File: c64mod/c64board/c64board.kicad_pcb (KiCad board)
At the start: 2 copper layers, 24.1 x 53.3 mm, 12 parts, among them J1 Conn_02x10_Odd_Even, U1 VIC-II, U2 MIC5504-3.3YM5, U3 LVC257, U4 LVC245, U5 LVC245

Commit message: Finished C64 mod board
generate gerber files also for Rev. 1
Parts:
- added REF**: OSHW-Logo2_7.3x6mm_SilkScreen, Symbol:OSHW-Logo2_7.3x6mm_SilkScreen, B.Cu at (143.8, 59.2)
- moved J1 23.0 mm to (154.9, 91.4), turned to 180 degrees
- moved R1 0.76 mm to (153.2, 99.1)
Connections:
- C2 pad 2: Net-(C2-Pad2) -> GND
- C3 pad 2: Net-(C2-Pad2) -> GND
- C4 pad 2: Net-(C2-Pad2) -> GND
- C5 pad 2: Net-(C2-Pad2) -> GND
- J1 pad 1: DB7 -> PHI0
- J1 pad 10: DB10_A4 -> DB9_A3
- J1 pad 11: DB9_A3 -> DB10_A4
- J1 pad 12: DB8_A2 -> DB11_A5
- J1 pad 13: A1 -> DB0
- J1 pad 14: A0 -> DB1
- J1 pad 15: CS -> DB2
- J1 pad 16: RW -> DB3
- J1 pad 17: BA -> DB4
- J1 pad 18: AEC -> DB5
- J1 pad 19: GND -> DB6
- J1 pad 2: DB6 -> GND
- J1 pad 20: PHI0 -> DB7
- J1 pad 3: DB5 -> AEC
- J1 pad 4: DB4 -> BA
- J1 pad 5: DB3 -> RW
- J1 pad 6: DB2 -> CS
- J1 pad 7: DB1 -> A0
- J1 pad 8: DB0 -> A1
- J1 pad 9: DB11_A5 -> DB8_A2
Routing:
- net Net-(U1-Pad27): track 0.00 -> 18.9 mm, vias 0 -> 3
- net GND: track 8.83 -> 27.2 mm, vias 3 -> 12
- net Net-(U1-Pad26): track 0.00 -> 15.4 mm, vias 0 -> 3
- net DB11_A5: track 0.00 -> 15.1 mm, vias 0 -> 1
- net DB9_A3: track 0.00 -> 14.3 mm, vias 0 -> 1
- net Net-(U1-Pad28): track 0.00 -> 13.9 mm, vias 0 -> 1
- net DB10_A4: track 0.00 -> 10.9 mm, vias 0 -> 2
- net +3V3: track 68.7 -> 65.7 mm
- net DB0: track 15.5 -> 18.4 mm
- net DB7: track 15.9 -> 13.7 mm
- net Net-(U1-Pad36): track 26.7 -> 25.5 mm
- net Net-(U1-Pad29): track 15.5 -> 16.7 mm
- net PHI0: track 7.01 -> 8.08 mm
- net BA: track 16.7 -> 15.7 mm
- net AEC: track 42.2 -> 41.6 mm
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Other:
- board text added: "1"
- board text added: "C64 mod Rev 1 github.com/c0pperdragon"

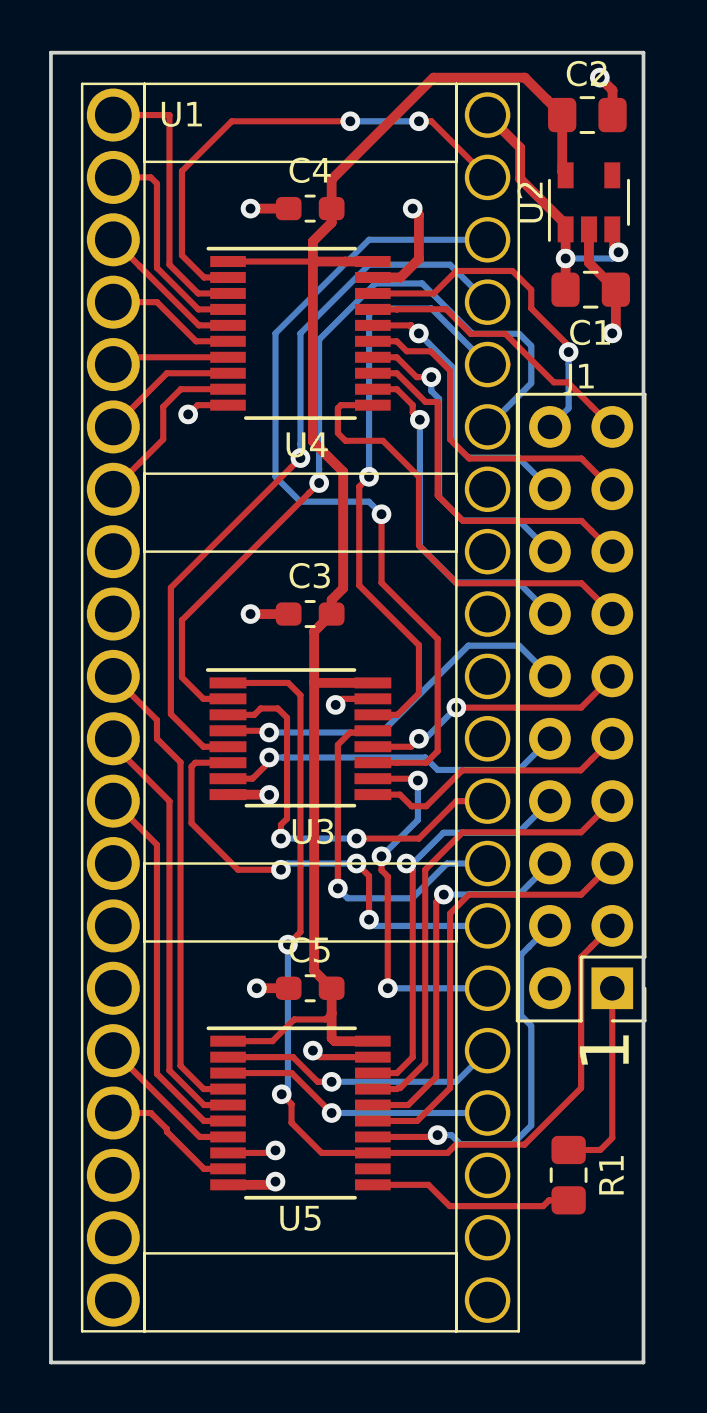
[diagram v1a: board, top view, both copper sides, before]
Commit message: Reverse connector orientation
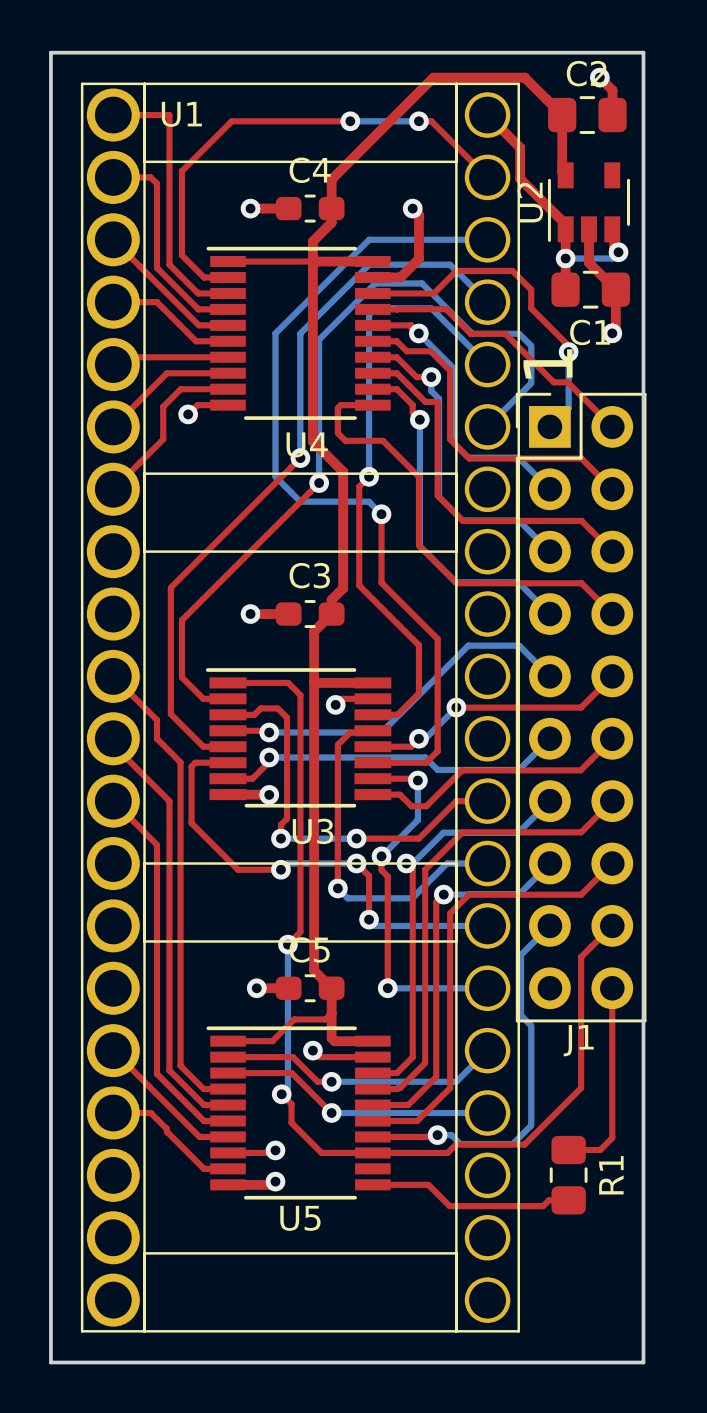
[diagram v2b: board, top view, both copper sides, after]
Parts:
- moved J1 23.0 mm to (152.4, 68.6), turned to 0 degrees
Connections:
- J1 pad 1: PHI0 -> DB7
- J1 pad 10: DB9_A3 -> DB10_A4
- J1 pad 11: DB10_A4 -> DB9_A3
- J1 pad 12: DB11_A5 -> DB8_A2
- J1 pad 13: DB0 -> A1
- J1 pad 14: DB1 -> A0
- J1 pad 15: DB2 -> CS
- J1 pad 16: DB3 -> RW
- J1 pad 17: DB4 -> BA
- J1 pad 18: DB5 -> AEC
- J1 pad 19: DB6 -> GND
- J1 pad 2: GND -> DB6
- J1 pad 20: DB7 -> PHI0
- J1 pad 3: AEC -> DB5
- J1 pad 4: BA -> DB4
- J1 pad 5: RW -> DB3
- J1 pad 6: CS -> DB2
- J1 pad 7: A0 -> DB1
- J1 pad 8: A1 -> DB0
- J1 pad 9: DB8_A2 -> DB11_A5
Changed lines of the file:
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@@
   )
   (module Connector_PinHeader_2.54mm:PinHeader_2x10_P2.54mm_Vertical (layer F.Cu)
-    (at 154.94 91.44 180)
+    (at 152.4 68.58)
     (descr "Through hole straight pin header, 2x10, 2.54mm pitch, double rows")
     (tags "Through hole pin header THT 2x10 2.54mm double row")
-    (fp_text reference J1 (at 1.27 24.892 180) (layer F.SilkS)
-      (effects (font (size 1 1) (thickness 0.15)))
-    )
-    (fp_text value Conn_02x10_Odd_Even (at 1.27 25.19 180) (layer F.Fab)
+    (fp_text reference J1 (at 1.27 24.892) (layer F.SilkS)
+      (effects (font (size 1 1) (thickness 0.15)))
+    )
+    (fp_text value Conn_02x10_Odd_Even (at 1.27 25.19) (layer F.Fab)
       (effects (font (size 1 1) (thickness 0.15)))
     )
@@
     (fp_line (start 4.35 24.65) (end 4.35 -1.8) (layer F.CrtYd) (width 0.05))
     (fp_line (start 4.35 -1.8) (end -1.8 -1.8) (layer F.CrtYd) (width 0.05))
-    (fp_text user %R (at 1.27 11.43 270) (layer F.Fab)
-      (effects (font (size 1 1) (thickness 0.15)))
-    )
-    (pad 1 thru_hole rect (at 0 0 180) (size 1.7 1.7) (drill 1) (layers *.Cu *.Mask)
+    (fp_text user %R (at 1.27 11.43 90) (layer F.Fab)
+      (effects (font (size 1 1) (thickness 0.15)))
+    )
+    (pad 1 thru_hole rect (at 0 0) (size 1.7 1.7) (drill 1) (layers *.Cu *.Mask)
+      (net 4 DB7))
+    (pad 2 thru_hole oval (at 2.54 0) (size 1.7 1.7) (drill 1) (layers *.Cu *.Mask)
+      (net 5 DB6))
+    (pad 3 thru_hole oval (at 0 2.54) (size 1.7 1.7) (drill 1) (layers *.Cu *.Mask)
+      (net 6 DB5))
+    (pad 4 thru_hole oval (at 2.54 2.54) (size 1.7 1.7) (drill 1) (layers *.Cu *.Mask)
+      (net 7 DB4))
+    (pad 5 thru_hole oval (at 0 5.08) (size 1.7 1.7) (drill 1) (layers *.Cu *.Mask)
+      (net 8 DB3))
+    (pad 6 thru_hole oval (at 2.54 5.08) (size 1.7 1.7) (drill 1) (layers *.Cu *.Mask)
+      (net 9 DB2))
+    (pad 7 thru_hole oval (at 0 7.62) (size 1.7 1.7) (drill 1) (layers *.Cu *.Mask)
+      (net 10 DB1))
+    (pad 8 thru_hole oval (at 2.54 7.62) (size 1.7 1.7) (drill 1) (layers *.Cu *.Mask)
+      (net 11 DB0))
+    (pad 9 thru_hole oval (at 0 10.16) (size 1.7 1.7) (drill 1) (layers *.Cu *.Mask)
+      (net 12 DB11_A5))
+    (pad 10 thru_hole oval (at 2.54 10.16) (size 1.7 1.7) (drill 1) (layers *.Cu *.Mask)
+      (net 13 DB10_A4))
+    (pad 11 thru_hole oval (at 0 12.7) (size 1.7 1.7) (drill 1) (layers *.Cu *.Mask)
+      (net 14 DB9_A3))
+    (pad 12 thru_hole oval (at 2.54 12.7) (size 1.7 1.7) (drill 1) (layers *.Cu *.Mask)
+      (net 15 DB8_A2))
+    (pad 13 thru_hole oval (at 0 15.24) (size 1.7 1.7) (drill 1) (layers *.Cu *.Mask)
+      (net 16 A1))
+    (pad 14 thru_hole oval (at 2.54 15.24) (size 1.7 1.7) (drill 1) (layers *.Cu *.Mask)
+      (net 17 A0))
+    (pad 15 thru_hole oval (at 0 17.78) (size 1.7 1.7) (drill 1) (layers *.Cu *.Mask)
+      (net 18 CS))
+    (pad 16 thru_hole oval (at 2.54 17.78) (size 1.7 1.7) (drill 1) (layers *.Cu *.Mask)
+      (net 19 RW))
+    (pad 17 thru_hole oval (at 0 20.32) (size 1.7 1.7) (drill 1) (layers *.Cu *.Mask)
+      (net 20 BA))
+    (pad 18 thru_hole oval (at 2.54 20.32) (size 1.7 1.7) (drill 1) (layers *.Cu *.Mask)
+      (net 21 AEC))
+    (pad 19 thru_hole oval (at 0 22.86) (size 1.7 1.7) (drill 1) (layers *.Cu *.Mask)
+      (net 2 GND))
+    (pad 20 thru_hole oval (at 2.54 22.86) (size 1.7 1.7) (drill 1) (layers *.Cu *.Mask)
       (net 22 PHI0))
-    (pad 2 thru_hole oval (at 2.54 0 180) (size 1.7 1.7) (drill 1) (layers *.Cu *.Mask)
-      (net 2 GND))
-    (pad 3 thru_hole oval (at 0 2.54 180) (size 1.7 1.7) (drill 1) (layers *.Cu *.Mask)
-      (net 21 AEC))
-    (pad 4 thru_hole oval (at 2.54 2.54 180) (size 1.7 1.7) (drill 1) (layers *.Cu *.Mask)
-      (net 20 BA))
-    (pad 5 thru_hole oval (at 0 5.08 180) (size 1.7 1.7) (drill 1) (layers *.Cu *.Mask)
-      (net 19 RW))
-    (pad 6 thru_hole oval (at 2.54 5.08 180) (size 1.7 1.7) (drill 1) (layers *.Cu *.Mask)
-      (net 18 CS))
-    (pad 7 thru_hole oval (at 0 7.62 180) (size 1.7 1.7) (drill 1) (layers *.Cu *.Mask)
-      (net 17 A0))
-    (pad 8 thru_hole oval (at 2.54 7.62 180) (size 1.7 1.7) (drill 1) (layers *.Cu *.Mask)
-      (net 16 A1))
-    (pad 9 thru_hole oval (at 0 10.16 180) (size 1.7 1.7) (drill 1) (layers *.Cu *.Mask)
-      (net 15 DB8_A2))
-    (pad 10 thru_hole oval (at 2.54 10.16 180) (size 1.7 1.7) (drill 1) (layers *.Cu *.Mask)
-      (net 14 DB9_A3))
-    (pad 11 thru_hole oval (at 0 12.7 180) (size 1.7 1.7) (drill 1) (layers *.Cu *.Mask)
-      (net 13 DB10_A4))
-    (pad 12 thru_hole oval (at 2.54 12.7 180) (size 1.7 1.7) (drill 1) (layers *.Cu *.Mask)
-      (net 12 DB11_A5))
-    (pad 13 thru_hole oval (at 0 15.24 180) (size 1.7 1.7) (drill 1) (layers *.Cu *.Mask)
-      (net 11 DB0))
-    (pad 14 thru_hole oval (at 2.54 15.24 180) (size 1.7 1.7) (drill 1) (layers *.Cu *.Mask)
-      (net 10 DB1))
-    (pad 15 thru_hole oval (at 0 17.78 180) (size 1.7 1.7) (drill 1) (layers *.Cu *.Mask)
-      (net 9 DB2))
-    (pad 16 thru_hole oval (at 2.54 17.78 180) (size 1.7 1.7) (drill 1) (layers *.Cu *.Mask)
-      (net 8 DB3))
-    (pad 17 thru_hole oval (at 0 20.32 180) (size 1.7 1.7) (drill 1) (layers *.Cu *.Mask)
-      (net 7 DB4))
-    (pad 18 thru_hole oval (at 2.54 20.32 180) (size 1.7 1.7) (drill 1) (layers *.Cu *.Mask)
-      (net 6 DB5))
-    (pad 19 thru_hole oval (at 0 22.86 180) (size 1.7 1.7) (drill 1) (layers *.Cu *.Mask)
-      (net 5 DB6))
-    (pad 20 thru_hole oval (at 2.54 22.86 180) (size 1.7 1.7) (drill 1) (layers *.Cu *.Mask)
-      (net 4 DB7))
     (model ${KISYS3DMOD}/Connector_PinHeader_2.54mm.3dshapes/PinHeader_2x10_P2.54mm_Vertical.wrl
       (at (xyz 0 0 0))
@@
       (xy -2.549664 -1.91989) (xy -2.469928 -1.911165) (xy -2.400256 -1.919918)) (layer B.SilkS) (width 0.01))
   )
-  (gr_text 1 (at 154.686 93.98 90) (layer F.SilkS)
+  (gr_text 1 (at 152.4 66.04 90) (layer F.SilkS)
     (effects (font (size 2 2) (thickness 0.3)))
   )
